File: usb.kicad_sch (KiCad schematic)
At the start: 17 parts, among them J201 USB_C_Receptacle_USB2.0_16P, J202 Screw_Terminal_01x02, Q1 STL6N3LLH6, U5 TCPP01-M12, U6 USBLC6-2P6, U7 STEF05SGR

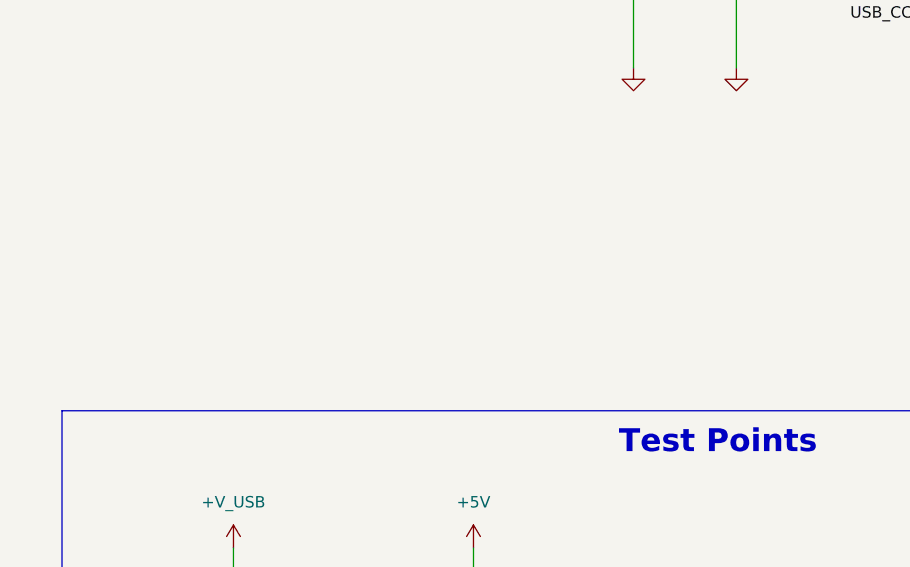
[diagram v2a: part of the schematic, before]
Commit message: routed board power supply
1. USB
2. LDO for DCDC_1 and DCDC_2
3. LDO for +1V2
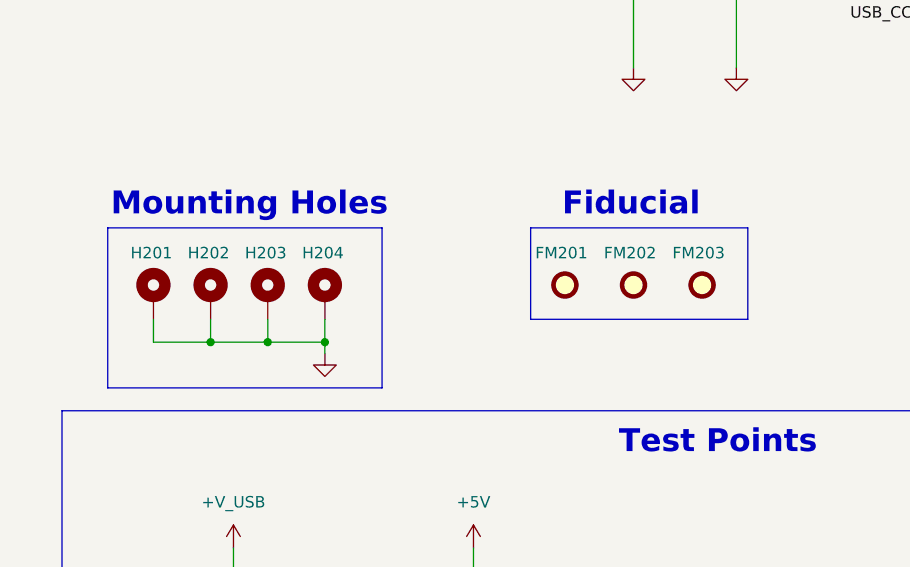
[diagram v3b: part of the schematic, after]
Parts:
- added FM201, FM202, FM203: Fiducial, Fiducial:Fiducial_1mm_Mask2mm, symbol Mechanical:Fiducial
- added H201, H202, H203, H204: MountingHole_Pad, MountingHole:MountingHole_3.2mm_M3_Pad, symbol Mechanical:MountingHole_Pad
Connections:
- net GND: now also H201.1, H202.1, H203.1, H204.1
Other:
- note added: "Fiducial"
- note added: "Mounting Holes"

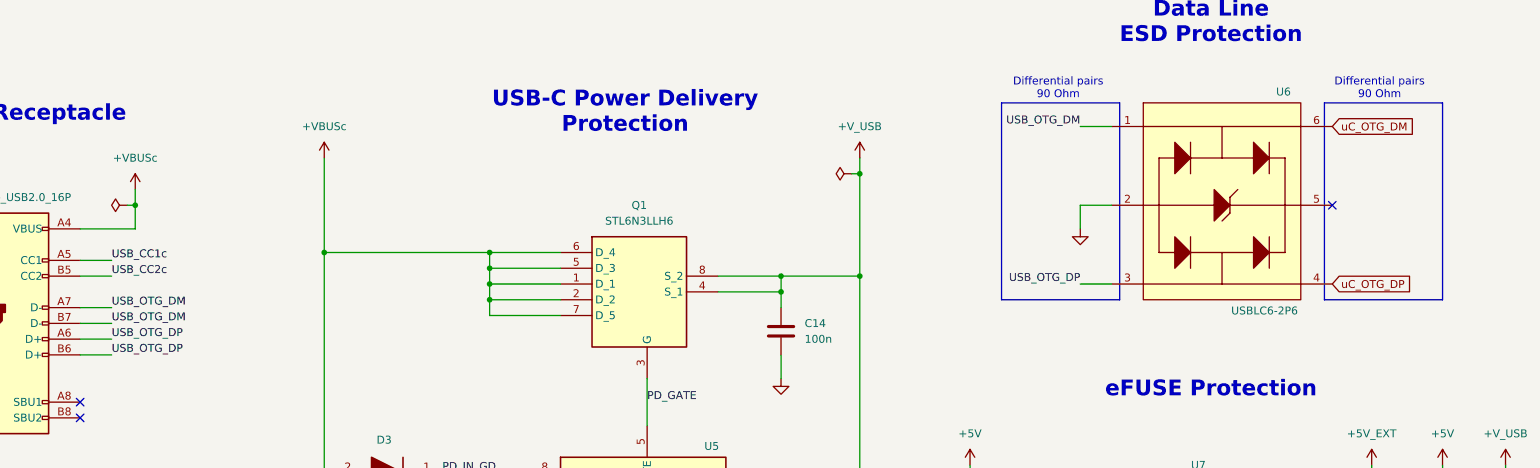
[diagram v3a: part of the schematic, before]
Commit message: routing for blueNRG complete
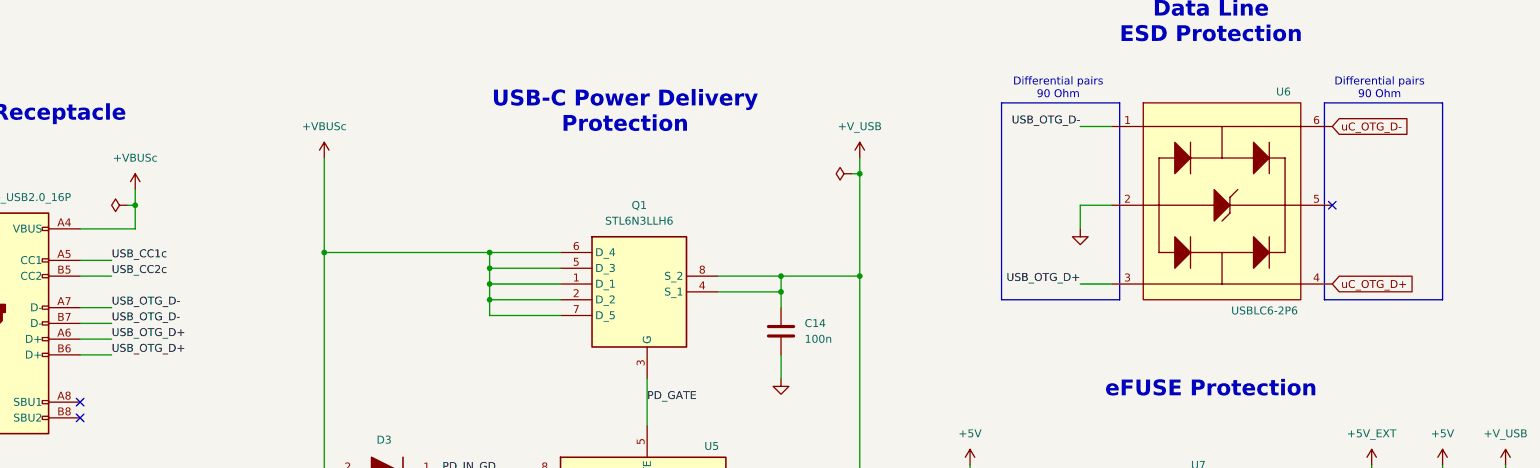
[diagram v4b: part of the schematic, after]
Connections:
- net USB_OTG_DM renamed USB_OTG_D-
- net USB_OTG_DP renamed USB_OTG_D+
- net uC_OTG_DM renamed uC_OTG_D-
- net uC_OTG_DP renamed uC_OTG_D+
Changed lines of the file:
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@@
 		)
 	)
-	(label "USB_OTG_DM"
+	(label "USB_OTG_D-"
 		(at 53.34 72.39 0)
 		(fields_autoplaced yes)
@@
 		)
 	)
-	(label "USB_OTG_DM"
+	(label "USB_OTG_D-"
 		(at 53.34 74.93 0)
 		(fields_autoplaced yes)
@@
 		)
 	)
-	(label "USB_OTG_DP"
+	(label "USB_OTG_D+"
 		(at 53.34 80.01 0)
 		(fields_autoplaced yes)
@@
 		)
 	)
-	(label "USB_OTG_DM"
+	(label "USB_OTG_D-"
 		(at 209.55 43.18 180)
 		(fields_autoplaced yes)
@@
 		)
 	)
-	(label "USB_OTG_DP"
+	(label "USB_OTG_D+"
 		(at 53.34 77.47 0)
 		(fields_autoplaced yes)
@@
 		)
 	)
-	(label "USB_OTG_DP"
+	(label "USB_OTG_D+"
 		(at 209.55 68.58 180)
 		(fields_autoplaced yes)
@@
 		)
 	)
-	(global_label "uC_OTG_DM"
+	(global_label "uC_OTG_D-"
 		(shape input)
 		(at 250.19 43.18 0)
@@
 		)
 		(property "Intersheetrefs" "${INTERSHEET_REFS}"
-			(at 263.8189 43.18 0)
+			(at 263.9399 43.18 0)
 			(effects
 				(font
@@
 		)
 	)
-	(global_label "uC_OTG_DP"
+	(global_label "uC_OTG_D+"
 		(shape input)
 		(at 250.19 68.58 0)
@@
 		)
 		(property "Intersheetrefs" "${INTERSHEET_REFS}"
-			(at 263.6375 68.58 0)
+			(at 263.9399 68.58 0)
 			(effects
 				(font

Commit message: finalized design v1.0.0
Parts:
- J201: Distributor_Link https://www.mouser.com/ProductDetail/Hirose-Connector/CX90B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 -> https://www.mouser.com/ProductDetail/GCT/USB4105-GF-A?qs=KU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; Manufacturer_Name Hirose Connector -> GCT; Manufacturer_Part_Number CX90B-16P -> USB4105-GF-A
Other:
- company: (none) -> Manufacturing Innovation Network Laboratory (MINLab)
- title: (none) -> Energy Monitoring System
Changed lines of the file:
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@@
 	(generator_version "8.0")
 	(paper "A4")
+	(title_block
+		(title "Energy Monitoring System")
+		(rev "v1.0.0")
+		(company "Manufacturing Innovation Network Laboratory (MINLab)")
+		(comment 1 "Developed by Vignesh Selvaraj")
+	)
 	(junction
 		(at 166.37 115.57)
@@
 			)
 		)
-		(property "Datasheet" "https://www.phoenixcontact.com/us/products/1548128/pdf"
+		(property "Datasheet" "https://www.mouser.com/manufacturer/phoenix-contact/"
 			(at 238.76 157.48 0)
 			(effects
@@
 			)
 		)
-		(property "Distributor_Link" "https://www.mouser.com/ProductDetail/Hirose-Connector/CX90B-16P?qs=vmHwEFxEFR%2Fiaz3BzOVsSQ%3D%3D"
+		(property "Distributor_Link" "https://www.mouser.com/ProductDetail/GCT/USB4105-GF-A?qs=KUoIvG%2F9IlY%2FMLlBMpStpA%3D%3D"
 			(at 33.02 74.93 0)
 			(effects
@@
 			)
 		)
-		(property "Manufacturer_Name" "Hirose Connector"
+		(property "Manufacturer_Name" "GCT"
 			(at 33.02 74.93 0)
 			(effects
@@
 			)
 		)
-		(property "Manufacturer_Part_Number" "CX90B-16P"
+		(property "Manufacturer_Part_Number" "USB4105-GF-A "
 			(at 33.02 74.93 0)
 			(effects

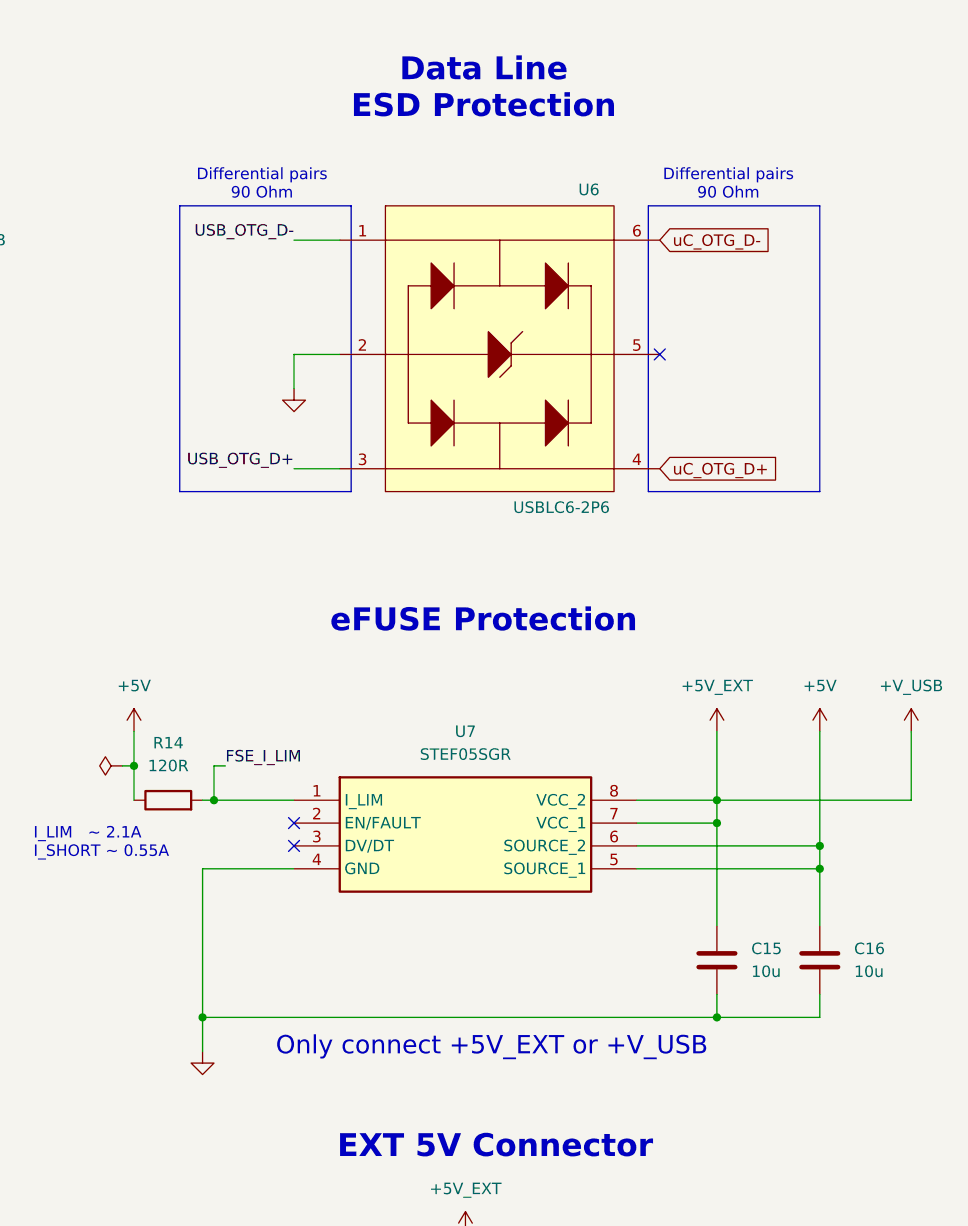
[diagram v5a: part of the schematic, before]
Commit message: v2.0 schematics updated
1. Need to be tested for errors
2. PCB layout is not started yet
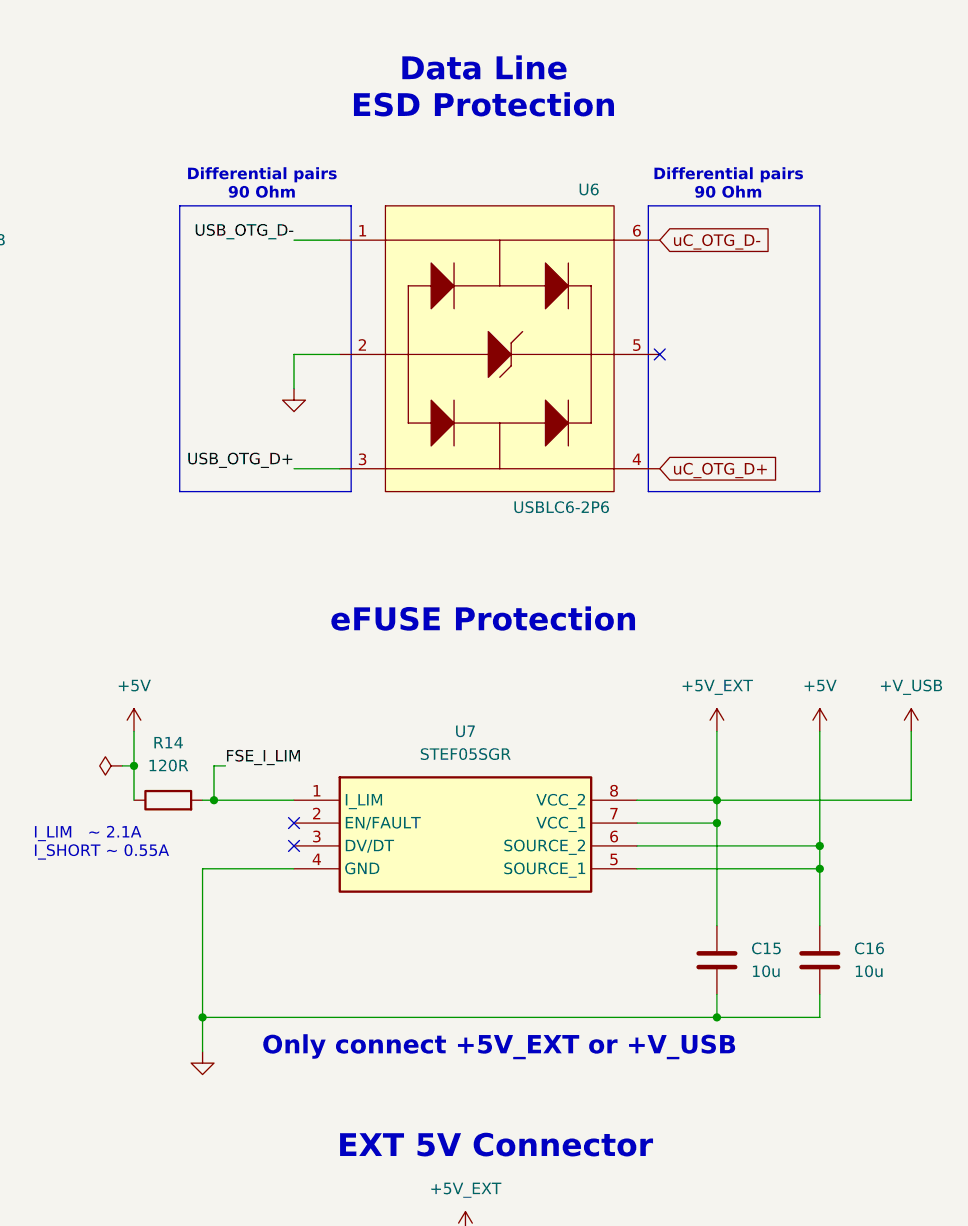
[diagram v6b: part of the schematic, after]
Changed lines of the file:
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@@
 			(font
 				(size 1.27 1.27)
+				(thickness 0.254)
+				(bold yes)
 			)
 		)
@@
 			(font
 				(size 1.27 1.27)
+				(thickness 0.254)
+				(bold yes)
 			)
 		)
@@
 	(text "Only connect +5V_EXT or +V_USB"
 		(exclude_from_sim no)
-		(at 207.518 132.842 0)
+		(at 205.994 132.842 0)
 		(effects
 			(font
 				(size 2.032 2.032)
+				(thickness 0.4064)
+				(bold yes)
+				(color 215 14 0 1)
 			)
 			(justify left)

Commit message: minor formatting updates
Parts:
- TP4, TP5: footprint EMS:5000 -> TestPoint:TestPoint_Pad_D3.0mm
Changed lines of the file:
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@@
 			(project ""
 				(path "/e660428c-c9b7-476c-8ac8-2d419f233469/7dd15615-8075-471d-b8bf-599b8660331d"
-					(reference "#PWR0209")
+					(reference "#PWR0220")
 					(unit 1)
 				)
@@
 			(project ""
 				(path "/e660428c-c9b7-476c-8ac8-2d419f233469/7dd15615-8075-471d-b8bf-599b8660331d"
-					(reference "#PWR0210")
+					(reference "#PWR0202")
 					(unit 1)
 				)
@@
 			(project ""
 				(path "/e660428c-c9b7-476c-8ac8-2d419f233469/7dd15615-8075-471d-b8bf-599b8660331d"
-					(reference "#PWR0213")
+					(reference "#PWR0208")
 					(unit 1)
 				)
@@
 			(project ""
 				(path "/e660428c-c9b7-476c-8ac8-2d419f233469/7dd15615-8075-471d-b8bf-599b8660331d"
-					(reference "#PWR0212")
+					(reference "#PWR0206")
 					(unit 1)
 				)
@@
 			(project ""
 				(path "/e660428c-c9b7-476c-8ac8-2d419f233469/7dd15615-8075-471d-b8bf-599b8660331d"
-					(reference "#PWR0207")
+					(reference "#PWR0218")
 					(unit 1)
 				)
@@
 			(project ""
 				(path "/e660428c-c9b7-476c-8ac8-2d419f233469/7dd15615-8075-471d-b8bf-599b8660331d"
-					(reference "D202")
+					(reference "D201")
 					(unit 1)
 				)
@@
 			(project ""
 				(path "/e660428c-c9b7-476c-8ac8-2d419f233469/7dd15615-8075-471d-b8bf-599b8660331d"
-					(reference "#PWR0220")
+					(reference "#PWR0205")
 					(unit 1)
 				)
@@
 			(project ""
 				(path "/e660428c-c9b7-476c-8ac8-2d419f233469/7dd15615-8075-471d-b8bf-599b8660331d"
-					(reference "D201")
+					(reference "D202")
 					(unit 1)
 				)
@@
 			(project ""
 				(path "/e660428c-c9b7-476c-8ac8-2d419f233469/7dd15615-8075-471d-b8bf-599b8660331d"
-					(reference "#PWR0208")
+					(reference "#PWR0219")
 					(unit 1)
 				)
@@
 			(project ""
 				(path "/e660428c-c9b7-476c-8ac8-2d419f233469/7dd15615-8075-471d-b8bf-599b8660331d"
-					(reference "#PWR0219")
+					(reference "#PWR0201")
 					(unit 1)
 				)
@@
 			(project ""
 				(path "/e660428c-c9b7-476c-8ac8-2d419f233469/7dd15615-8075-471d-b8bf-599b8660331d"
-					(reference "#FLG0203")
+					(reference "#FLG0204")
 					(unit 1)
 				)
@@
 			(project ""
 				(path "/e660428c-c9b7-476c-8ac8-2d419f233469/7dd15615-8075-471d-b8bf-599b8660331d"
-					(reference "#PWR0206")
+					(reference "#PWR0213")
 					(unit 1)
 				)
@@
 			(project ""
 				(path "/e660428c-c9b7-476c-8ac8-2d419f233469/7dd15615-8075-471d-b8bf-599b8660331d"
-					(reference "#PWR0211")
+					(reference "#PWR0209")
 					(unit 1)
 				)
@@
 			(project ""
 				(path "/e660428c-c9b7-476c-8ac8-2d419f233469/7dd15615-8075-471d-b8bf-599b8660331d"
-					(reference "#PWR0201")
+					(reference "#PWR0207")
 					(unit 1)
 				)
@@
 		(dnp no)
 		(fields_autoplaced yes)
-		(property "Reference" "#PWR0217"
+		(property "Reference" "#PWR0203"
 			(at 41.91 167.64 0)
 			(effects
@@
 			(project "EnergyMonitoringSystem"
 				(path "/e660428c-c9b7-476c-8ac8-2d419f233469/7dd15615-8075-471d-b8bf-599b8660331d"
-					(reference "#PWR0217")
+					(reference "#PWR0203")
 					(unit 1)
 				)
@@
 			(project ""
 				(path "/e660428c-c9b7-476c-8ac8-2d419f233469/7dd15615-8075-471d-b8bf-599b8660331d"
-					(reference "U201")
+					(reference "U203")
 					(unit 1)
 				)
@@
 			)
 		)
-		(property "Footprint" "EMS:5000"
+		(property "Footprint" "TestPoint:TestPoint_Pad_D3.0mm"
 			(at 52.07 185.42 0)
 			(effects
@@
 		(dnp no)
 		(fields_autoplaced yes)
-		(property "Reference" "#FLG0204"
+		(property "Reference" "#FLG0201"
 			(at 34.925 104.14 0)
 			(effects
@@
 			(project "EnergyMonitoringSystem"
 				(path "/e660428c-c9b7-476c-8ac8-2d419f233469/7dd15615-8075-471d-b8bf-599b8660331d"
-					(reference "#FLG0204")
+					(reference "#FLG0201")
 					(unit 1)
 				)
@@
 			(project ""
 				(path "/e660428c-c9b7-476c-8ac8-2d419f233469/7dd15615-8075-471d-b8bf-599b8660331d"
-					(reference "R202")
+					(reference "R203")
 					(unit 1)
 				)
@@
 			)
 		)
-		(property "Footprint" "EMS:5000"
+		(property "Footprint" "TestPoint:TestPoint_Pad_D3.0mm"
 			(at 24.13 185.42 0)
 			(effects
@@
 			(project ""
 				(path "/e660428c-c9b7-476c-8ac8-2d419f233469/7dd15615-8075-471d-b8bf-599b8660331d"
-					(reference "#PWR0204")
+					(reference "#PWR0215")
 					(unit 1)
 				)
@@
 			(project ""
 				(path "/e660428c-c9b7-476c-8ac8-2d419f233469/7dd15615-8075-471d-b8bf-599b8660331d"
-					(reference "U203")
+					(reference "U201")
 					(unit 1)
 				)
@@
 			(project ""
 				(path "/e660428c-c9b7-476c-8ac8-2d419f233469/7dd15615-8075-471d-b8bf-599b8660331d"
-					(reference "#PWR0218")
+					(reference "#PWR0217")
 					(unit 1)
 				)
@@
 			(project ""
 				(path "/e660428c-c9b7-476c-8ac8-2d419f233469/7dd15615-8075-471d-b8bf-599b8660331d"
-					(reference "#PWR0202")
+					(reference "#PWR0212")
 					(unit 1)
 				)
@@
 			(project ""
 				(path "/e660428c-c9b7-476c-8ac8-2d419f233469/7dd15615-8075-471d-b8bf-599b8660331d"
-					(reference "#PWR0205")
+					(reference "#PWR0210")
 					(unit 1)
 				)
@@
 			(project ""
 				(path "/e660428c-c9b7-476c-8ac8-2d419f233469/7dd15615-8075-471d-b8bf-599b8660331d"
-					(reference "#PWR0215")
+					(reference "#PWR0214")
 					(unit 1)
 				)
@@
 			(project ""
 				(path "/e660428c-c9b7-476c-8ac8-2d419f233469/7dd15615-8075-471d-b8bf-599b8660331d"
-					(reference "R203")
+					(reference "R202")
 					(unit 1)
 				)
@@
 			(project ""
 				(path "/e660428c-c9b7-476c-8ac8-2d419f233469/7dd15615-8075-471d-b8bf-599b8660331d"
-					(reference "C201")
+					(reference "C202")
 					(unit 1)
 				)
@@
 			(project ""
 				(path "/e660428c-c9b7-476c-8ac8-2d419f233469/7dd15615-8075-471d-b8bf-599b8660331d"
-					(reference "#PWR0203")
+					(reference "#PWR0204")
 					(unit 1)
 				)
@@
 			(project ""
 				(path "/e660428c-c9b7-476c-8ac8-2d419f233469/7dd15615-8075-471d-b8bf-599b8660331d"
-					(reference "C202")
+					(reference "C201")
 					(unit 1)
 				)
@@
 			(project ""
 				(path "/e660428c-c9b7-476c-8ac8-2d419f233469/7dd15615-8075-471d-b8bf-599b8660331d"
-					(reference "#PWR0214")
+					(reference "#PWR0211")
 					(unit 1)
 				)
@@
 			(project ""
 				(path "/e660428c-c9b7-476c-8ac8-2d419f233469/7dd15615-8075-471d-b8bf-599b8660331d"
-					(reference "#FLG0201")
+					(reference "#FLG0203")
 					(unit 1)
 				)
